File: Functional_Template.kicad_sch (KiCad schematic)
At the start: 12 parts

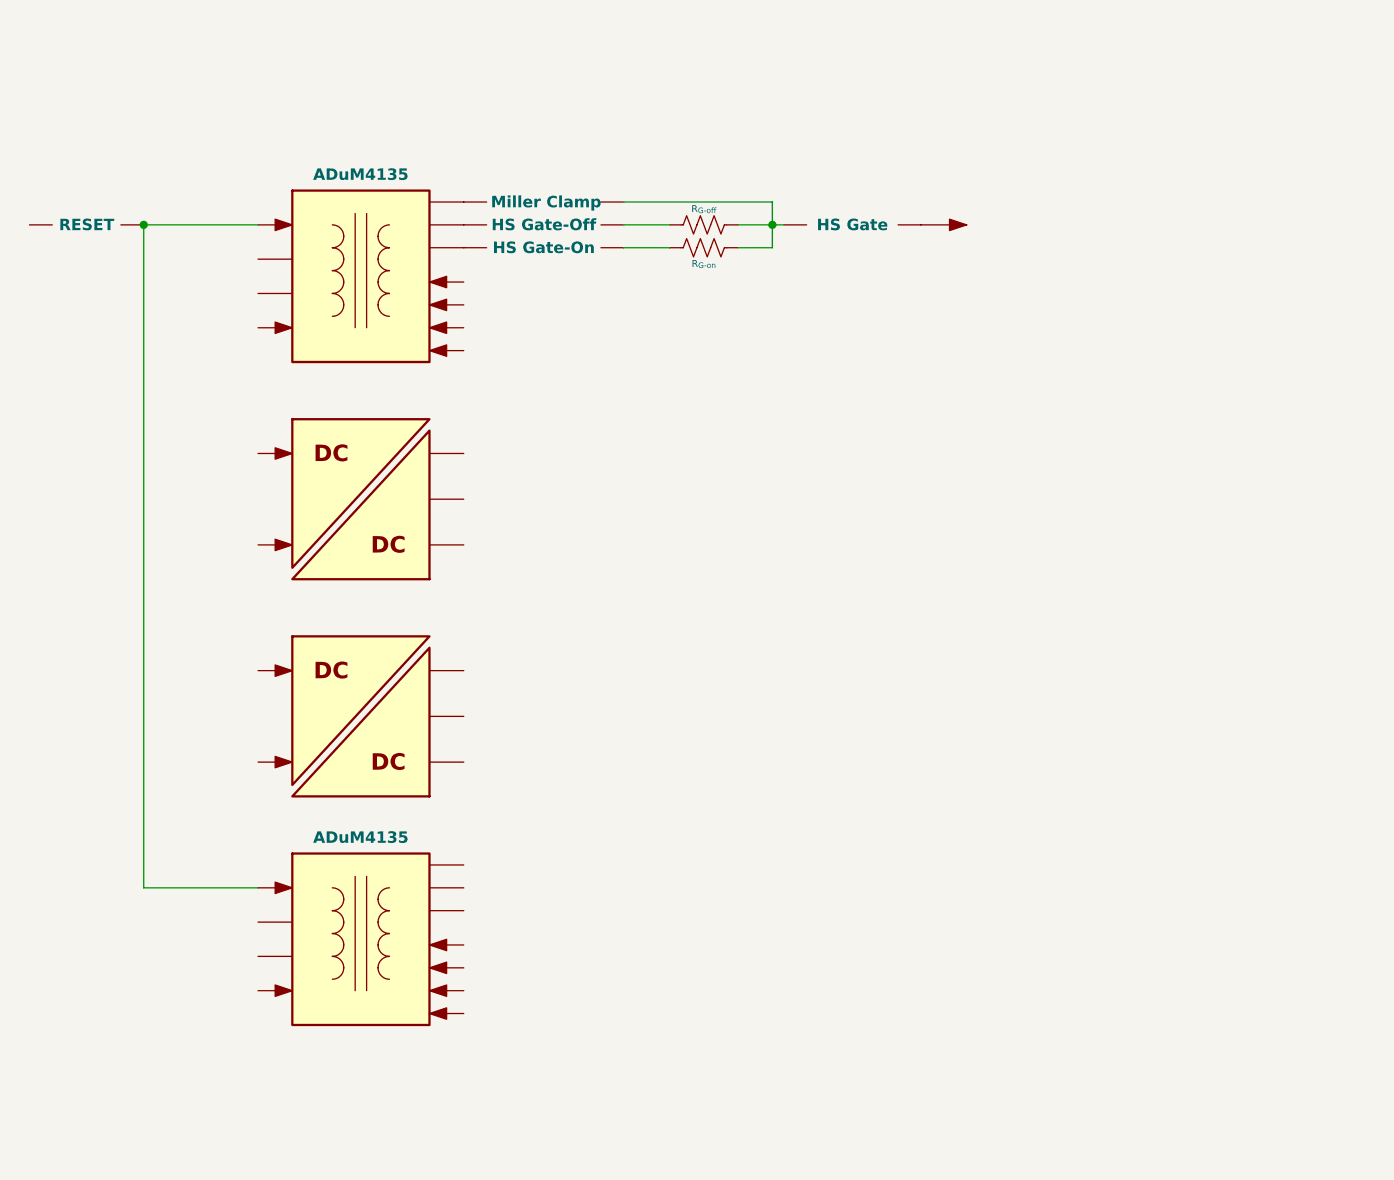
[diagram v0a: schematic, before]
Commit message: чуть наполнил библиотеку блоками
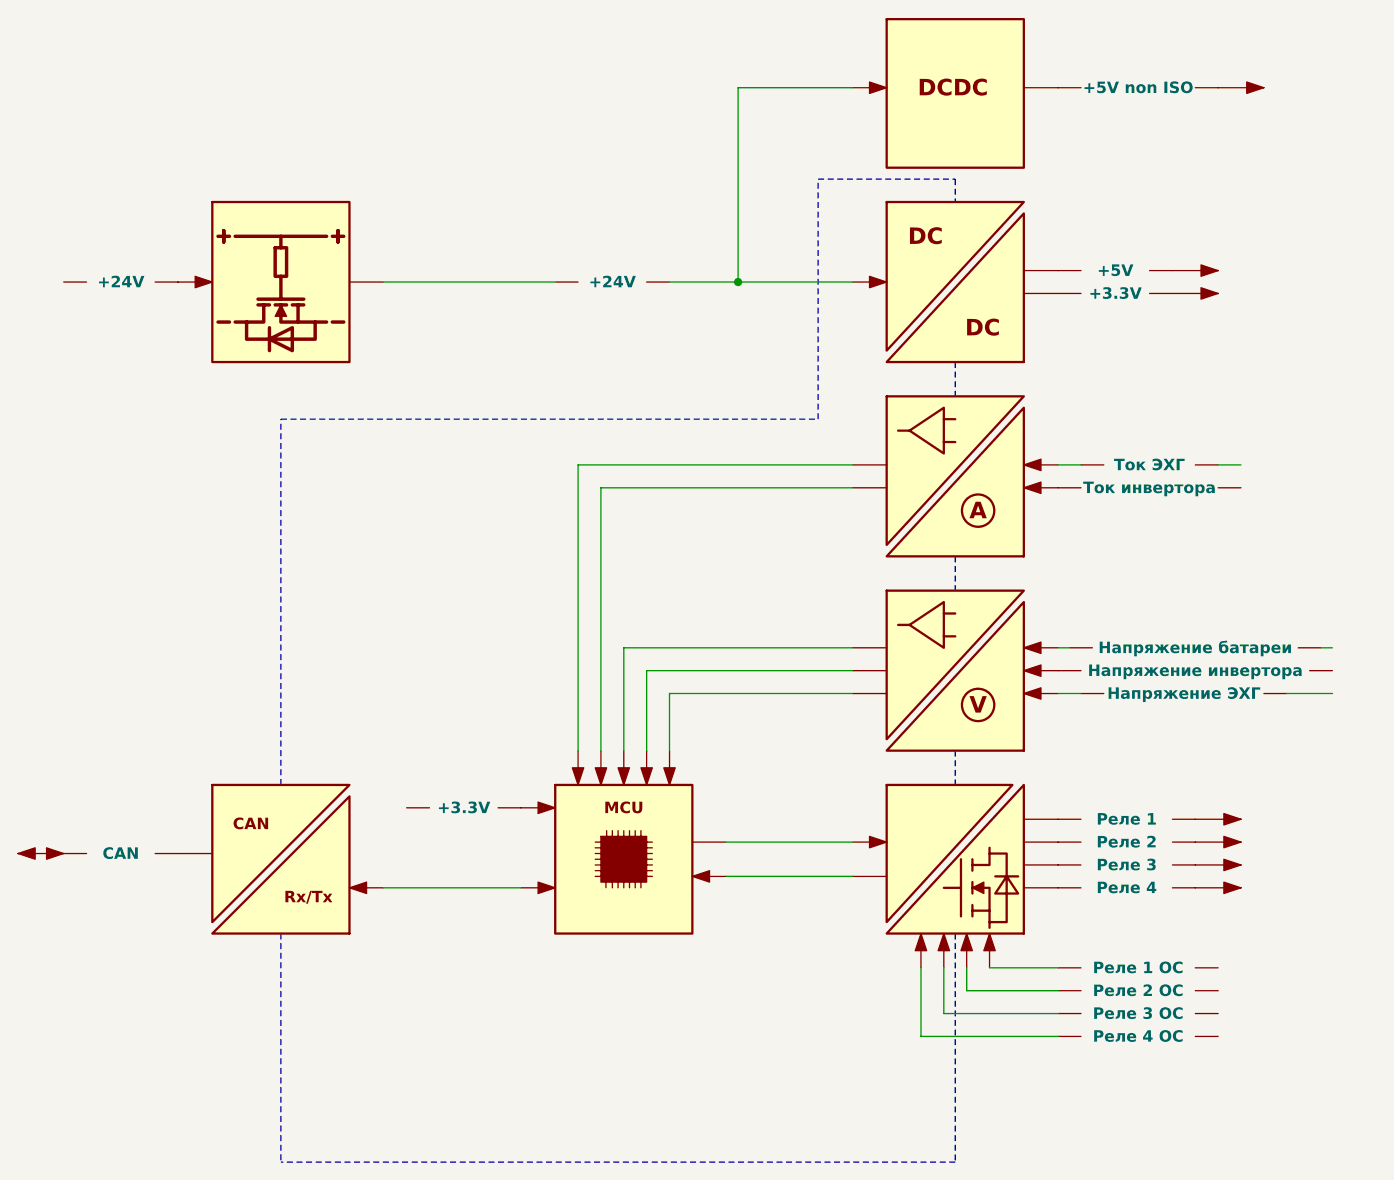
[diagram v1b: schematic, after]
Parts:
- removed D5: Miller Clamp, symbol Block_Template:Label
- removed D6: HS Gate-Off, symbol Block_Template:Label
- removed D7: HS Gate-On, symbol Block_Template:Label
- removed R1: R_{G-off}, symbol Device:R_US
- removed R2: R_{G-on}, symbol Device:R_US
- added D11: +5V, symbol Block_Template:Label
- added D12, D28: +3.3V, symbol Block_Template:Label
- added D13, D15, D17, D19, D21, D23, D36: (no value), symbol Block_Template:Arrow
- added D14: +5V non ISO, symbol Block_Template:Label
- added D16: Реле 1, symbol Block_Template:Label
- added D18: Реле 2, symbol Block_Template:Label
- added D20: Реле 3, symbol Block_Template:Label
- added D22: Реле 4, symbol Block_Template:Label
- added D24: Реле 1 ОС, symbol Block_Template:Label
- added D25: Реле 2 ОС, symbol Block_Template:Label
- added D26: Реле 3 ОС, symbol Block_Template:Label
- added D27: Реле 4 ОС, symbol Block_Template:Label
- added D29: Напряжение батареи, symbol Block_Template:Label
- added D30: Напряжение инвертора, symbol Block_Template:Label
- added D31: Напряжение ЭХГ, symbol Block_Template:Label
- added D32: Ток ЭХГ, symbol Block_Template:Label
- added D33: Ток инвертора, symbol Block_Template:Label
- added D34, D5, D7: ADuM4135, symbol Block_Template:Block
- added D35: CAN, symbol Block_Template:Label
- added D6: ADuM4135, symbol Block_Template:CAN_iso
- D1: value ADuM4135 -> (none)
- D10: value RESET -> +24V
- D9: value HS Gate -> +24V
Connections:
- net at D2.: now also D11.
- net at D4.: now also D7.
- net at D3.: now also D14.
- net at D1.: now also D9.
- net at D8.: now also D11.; no longer D9.
- net at D10.: now also D1.
- new net: D24., D5.
- new net: D31., D34.
- new net: D10., D2., D3.
- new net: D20., D5.
- new net: D20., D21.
- new net: D35., D6.
- new net: D35., D36.
- new net: D18., D19.
- new net: D29., D34.
- new net: D12., D2.
- new net: D30., D34.
- new net: D12., D13.
- new net: D27., D5.
- new net: D26., D5.
- new net: D18., D5.
- new net: D22., D5.
- new net: D25., D5.
- new net: D16., D5.
- new net: D4., D5. (x2)
- new net: D4., D6.
- new net: D14., D15.
- new net: D22., D23.
- new net: D16., D17.
- new net: D33., D7.
- new net: D28., D4.
- new net: D34., D4. (x3)
- new net: D4., D7.
- new net: D32., D7.
